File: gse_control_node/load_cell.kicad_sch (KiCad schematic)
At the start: 1 part, among them J3 Conn_01x04

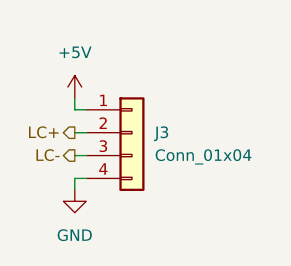
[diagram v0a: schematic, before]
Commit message: finish control board routing
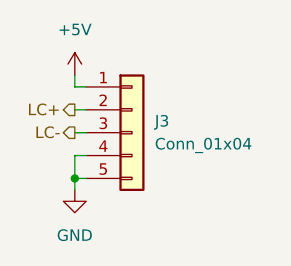
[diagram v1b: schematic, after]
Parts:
- J3: footprint Connector_Molex:Molex_Micro-Fit_3.0_43650-0415_1x04_P3.00mm_Vertical -> Connector_Molex:Molex_Micro-Fit_3.0_43650-0515_1x05_P3.00mm_Vertical; symbol Connector_Generic:Conn_01x04 -> Connector_Generic:Conn_01x05; now in the parts list
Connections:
- net GND: now also J3.5 (Pin_5)
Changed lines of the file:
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@@
 	(generator_version "10.0")
 	(paper "A5")
-	(wire
-		(pts
-			(xy 99.06 66.04) (xy 100.33 66.04)
-		)
-		(stroke
-			(width 0)
-			(type default)
-		)
-	)
-	(wire
-		(pts
-			(xy 99.06 59.69) (xy 99.06 60.96)
-		)
-		(stroke
-			(width 0)
-			(type default)
-		)
-	)
-	(wire
-		(pts
-			(xy 99.06 69.85) (xy 99.06 68.58)
+	(junction
+		(at 99.06 68.58)
+		(diameter 0)
+		(color 0 0 0 0)
+	)
+	(wire
+		(pts
+			(xy 99.06 60.96) (xy 100.33 60.96)
+		)
+		(stroke
+			(width 0)
+			(type default)
+		)
+	)
+	(wire
+		(pts
+			(xy 100.33 66.04) (xy 99.06 66.04)
+		)
+		(stroke
+			(width 0)
+			(type default)
+		)
+	)
+	(wire
+		(pts
+			(xy 99.06 58.42) (xy 100.33 58.42)
+		)
+		(stroke
+			(width 0)
+			(type default)
+		)
+	)
+	(wire
+		(pts
+			(xy 99.06 57.15) (xy 99.06 58.42)
+		)
+		(stroke
+			(width 0)
+			(type default)
+		)
+	)
+	(wire
+		(pts
+			(xy 99.06 66.04) (xy 99.06 68.58)
+		)
+		(stroke
+			(width 0)
+			(type default)
+		)
+	)
+	(wire
+		(pts
+			(xy 99.06 68.58) (xy 99.06 69.85)
 		)
 		(stroke
@@
 		(pts
 			(xy 99.06 63.5) (xy 100.33 63.5)
-		)
-		(stroke
-			(width 0)
-			(type default)
-		)
-	)
-	(wire
-		(pts
-			(xy 99.06 60.96) (xy 100.33 60.96)
 		)
 		(stroke
@@
 	(hierarchical_label "LC-"
 		(shape output)
-		(at 99.06 66.04 180)
+		(at 99.06 63.5 180)
 		(effects
 			(font
@@
 	(hierarchical_label "LC+"
 		(shape output)
-		(at 99.06 63.5 180)
+		(at 99.06 60.96 180)
 		(effects
 			(font
@@
 	(symbol
 		(lib_id "power:+5V")
-		(at 99.06 59.69 0)
+		(at 99.06 57.15 0)
 		(unit 1)
 		(body_style 1)
@@
 		(fields_autoplaced yes)
 		(property "Reference" "#PWR024"
-			(at 99.06 63.5 0)
+			(at 99.06 60.96 0)
 			(hide yes)
 			(show_name no)
@@
 		)
 		(property "Value" "+5V"
-			(at 99.06 54.61 0)
+			(at 99.06 52.07 0)
 			(show_name no)
 			(do_not_autoplace no)
@@
 		)
 		(property "Footprint" ""
-			(at 99.06 59.69 0)
+			(at 99.06 57.15 0)
 			(hide yes)
 			(show_name no)
@@
 		)
 		(property "Datasheet" ""
-			(at 99.06 59.69 0)
+			(at 99.06 57.15 0)
 			(hide yes)
 			(show_name no)
@@
 		)
 		(property "Description" "Power symbol creates a global label with name \"+5V\""
-			(at 99.06 59.69 0)
+			(at 99.06 57.15 0)
 			(hide yes)
 			(show_name no)
@@
 	)
 	(symbol
-		(lib_id "Connector_Generic:Conn_01x04")
+		(lib_id "Connector_Generic:Conn_01x05")
 		(at 105.41 63.5 0)
 		(unit 1)
 		(body_style 1)
 		(exclude_from_sim no)
-		(in_bom no)
+		(in_bom yes)
 		(on_board yes)
-		(in_pos_files no)
+		(in_pos_files yes)
 		(dnp no)
 		(fields_autoplaced yes)
 		(property "Reference" "J3"
-			(at 107.95 63.4999 0)
+			(at 107.95 62.2299 0)
 			(show_name no)
 			(do_not_autoplace no)
@@
 		)
 		(property "Value" "Conn_01x04"
-			(at 107.95 66.0399 0)
+			(at 107.95 64.7699 0)
 			(show_name no)
 			(do_not_autoplace no)
@@
 			)
 		)
-		(property "Footprint" "Connector_Molex:Molex_Micro-Fit_3.0_43650-0415_1x04_P3.00mm_Vertical"
+		(property "Footprint" "Connector_Molex:Molex_Micro-Fit_3.0_43650-0515_1x05_P3.00mm_Vertical"
 			(at 105.41 63.5 0)
 			(hide yes)
@@
 			)
 		)
-		(property "Description" "Generic connector, single row, 01x04, script generated (kicad-library-utils/schlib/autogen/connector/)"
+		(property "Description" "Generic connector, single row, 01x05, script generated (kicad-library-utils/schlib/autogen/connector/)"
 			(at 105.41 63.5 0)
 			(hide yes)
@@
 		(pin "3"
 		)
+		(pin "5"
+		)
 		(instances

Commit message: updates for manufacturing
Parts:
- J3: value Conn_01x04 -> Conn_01x05
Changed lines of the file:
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@@
 			)
 		)
-		(property "Value" "Conn_01x04"
+		(property "Value" "Conn_01x05"
 			(at 107.95 64.7699 0)
 			(show_name no)
